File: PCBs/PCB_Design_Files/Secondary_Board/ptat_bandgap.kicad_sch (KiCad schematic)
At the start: 0 parts

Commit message: ptat_bandgap schematic on secondary board
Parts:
- added C1: .1u, Project Footprints:0603_capacitor, symbol Project_Symbols:0603_capacitor
- added IC1: TLV2333IDGKR, Project Footprints:TLV2333IDGKR, symbol Project_Symbols:TLV2333IDGKR
- added Q1, Q2: DMMT3904W-7-F, Project Footprints:DMMT3904W_Dual_NPN, symbol Project_Symbols:DMMT3904W-7-F
- added R3: 40k, Project Footprints:0603_resistor, symbol Project_Symbols:0603_resistor
- added R4: 2.5k, Project Footprints:0603_resistor, symbol Project_Symbols:0603_resistor
- added R5: 5k, Project Footprints:0603_resistor, symbol Project_Symbols:0603_resistor
- added R6, R7: 1k, Project Footprints:0603_resistor, symbol Project_Symbols:0603_resistor
- added R8: 103, Project Footprints:0603_resistor, symbol Project_Symbols:0603_resistor
- added R9: 2040, Project Footprints:0603_resistor, symbol Project_Symbols:0603_resistor
- added U1, U2, U3, U4: DMMT5401-7-F, Project Footprints:DMMT5401_Dual_PNP, symbol Project_Symbols:DMMT5401-7-F
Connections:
- new net: R7.2, U4.5 (E2)
- new net: Q1.1 (B2), Q1.6 (C2), Q2.1 (B2), Q2.2 (B1), Q2.3 (C1), Q2.6 (C2), R8.2
- new net: IC1.2 (-IN_A), IC1.6 (-IN_B), Q1.2 (B1), Q1.3 (C1), U1.1 (C1), U2.4 (C2)
- new net: R3.1, U1.2 (B1), U1.4 (C2)
- new net: IC1.5 (+IN_B), R8.1, U2.1 (C1)
- new net: IC1.7 (OUT_B), U1.3 (B2), U2.2 (B1), U2.3 (B2), U3.2 (B1), U3.3 (B2)
- new net: R6.2, U4.6 (E1)
- new net: IC1.3 (+IN_A), R9.1, U4.4 (C2)
- new net: IC1.1 (OUT_A), U4.2 (B1), U4.3 (B2)
- new net +3V3: C1.2, IC1.8 (V+), R6.1, R7.1, U1.5 (E2), U1.6 (E1), U2.5 (E2), U2.6 (E1), U3.5 (E2), U3.6 (E1)
- new net GND: C1.1, IC1.4 (V-), Q1.4 (E1), Q1.5 (E2), Q2.4 (E1), Q2.5 (E2), R3.2, R4.2, R5.2, R9.2
- new net V_bandgap: R4.1, U3.4 (C2), U4.1 (C1)
- new net V_ptat: R5.1, U3.1 (C1)
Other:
- note added: "1x NPN"
- note added: "3x NPN"
- note added: "Bandgap"
- note added: "Bandgap-PTAT Circuit"
- note added: "PTAT"
- note added: "Startup"

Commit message: updated bg_ptat
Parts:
- added C8: .1u, Project Footprints:0603_capacitor, symbol Project_Symbols:0603_capacitor
- added U7: TLV9002, Project Footprints:TLV9002, symbol Project_Symbols:TLV9002
- R4: value 2.5k -> 2.2k
- R8: value 103 -> 105
- R9: value 2040 -> 2050
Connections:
- net +3V3: now also C8.2, U7.8 (V+)
- net GND: now also C8.1, U7.4 (V-)
- net V_bandgap: now also U7.6 (IN2-), U7.7 (OUT2); no longer R4.1, U3.4 (C2), U4.1 (C1)
- net V_ptat: now also U7.1 (OUT1), U7.2 (IN1-); no longer R5.1, U3.1 (C1)
- new net Vbg: R4.1, U3.4 (C2), U4.1 (C1), U7.5 (IN2+)
- new net Vptat: R5.1, U3.1 (C1), U7.3 (IN1+)
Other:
- note added: "Buffer Output"
- moved on the sheet: C1, IC1, Q1, Q2, R3, R4, R5, R6, R7, R8, R9, U1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

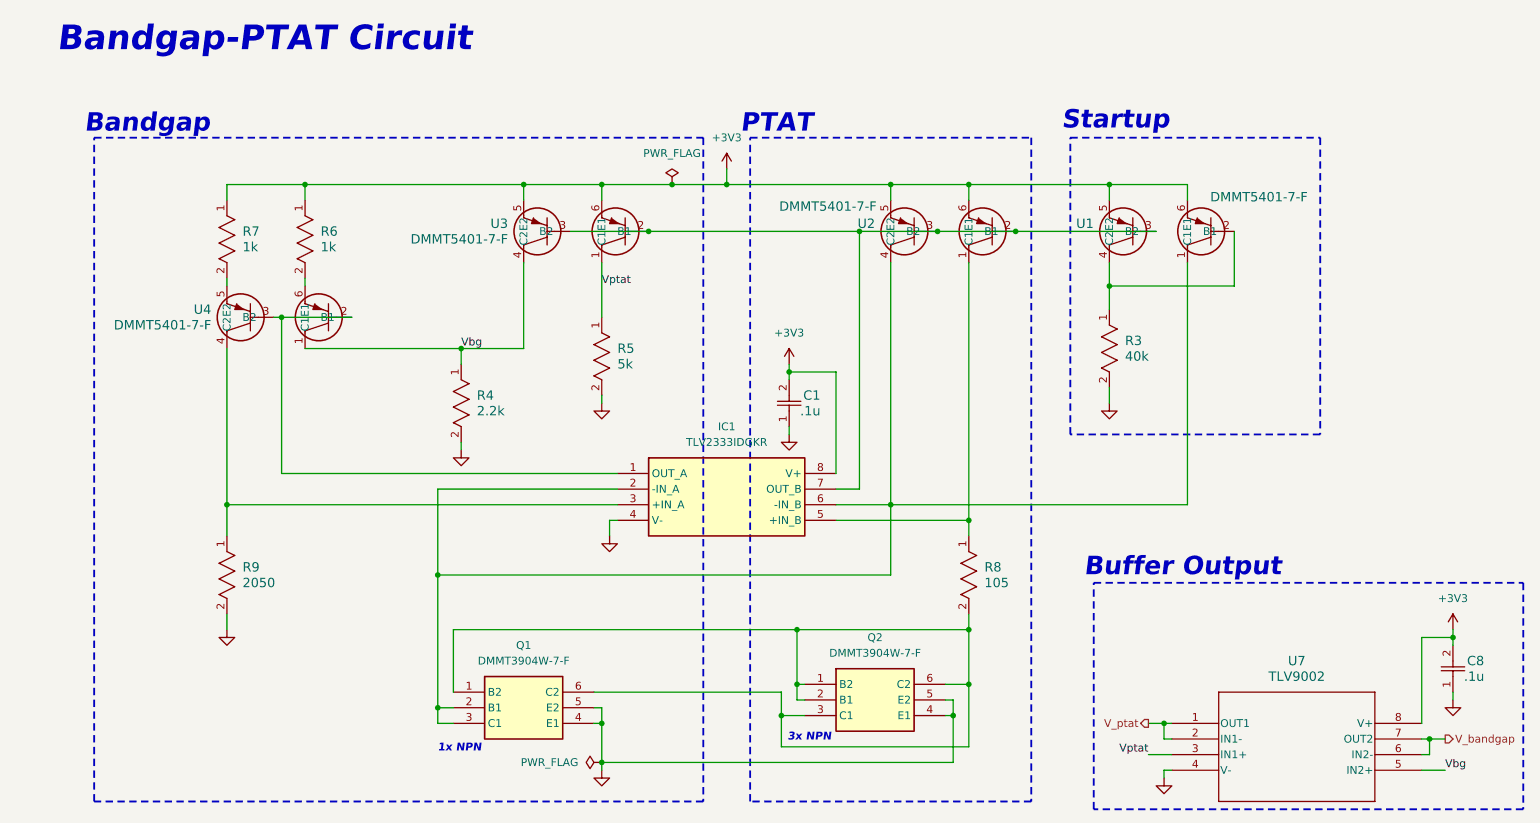
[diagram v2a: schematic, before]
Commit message: updated ptat_bandgap schematic and layout. Fixed +3v3 and +5V flags
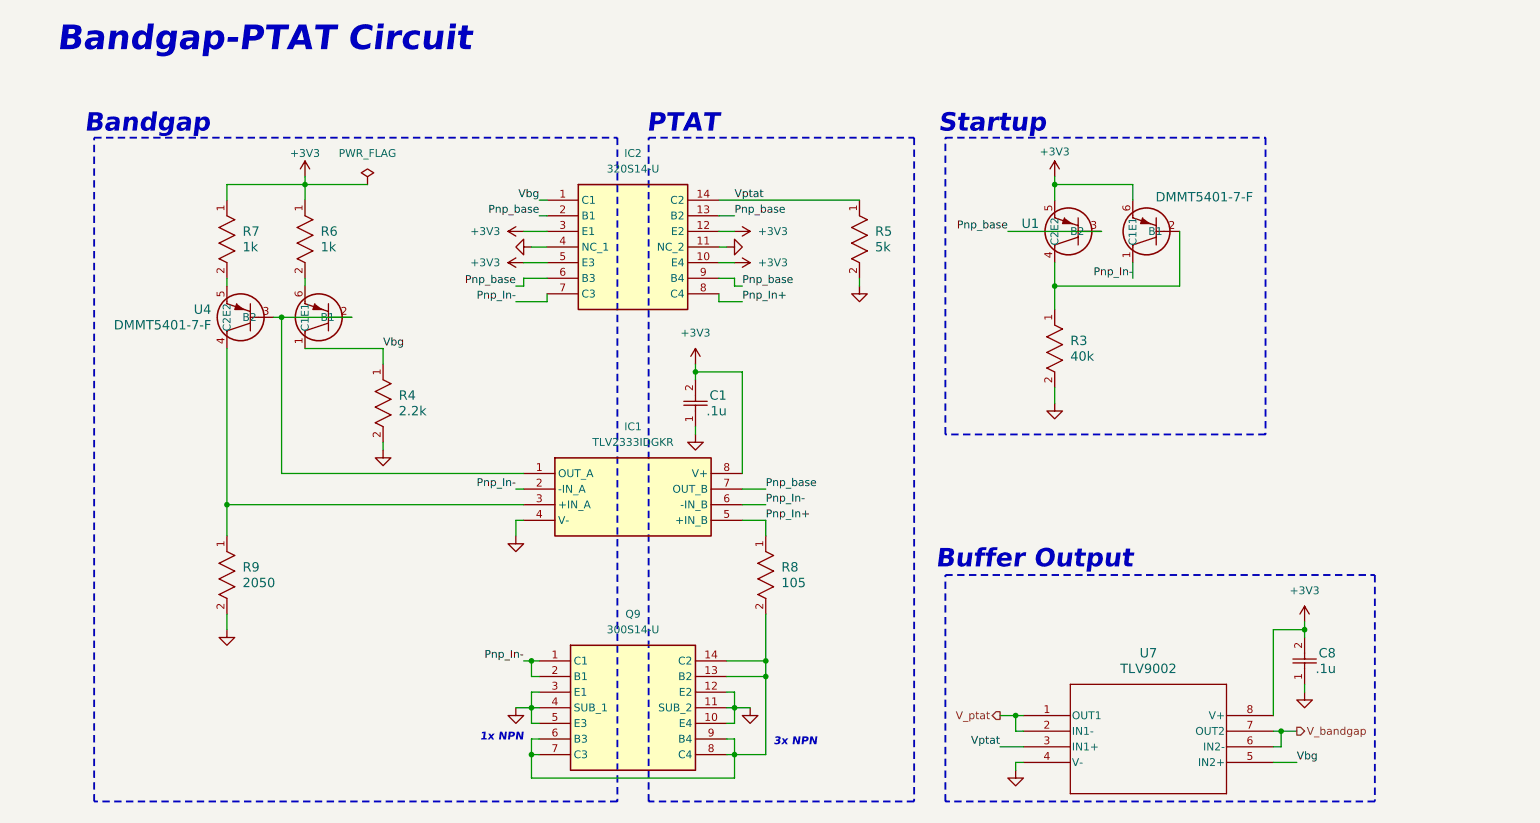
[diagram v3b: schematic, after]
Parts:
- removed Q1, Q2: DMMT3904W-7-F, Project Footprints:DMMT3904W_Dual_NPN, symbol Project_Symbols:DMMT3904W-7-F
- removed U2, U3: DMMT5401-7-F, Project Footprints:DMMT5401_Dual_PNP, symbol Project_Symbols:DMMT5401-7-F
- added IC2: 320S14-U, Project Footprints:That320_pnp, symbol Project_Symbols:320S14-U
- added Q9: 300S14-U, Project Footprints:That300_npn, symbol Project_Symbols:300S14-U
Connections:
- net +3V3: now also IC2.10 (E4), IC2.12 (E2), IC2.3 (E1), IC2.5 (E3)
- net GND: now also IC2.11 (NC_2), IC2.4 (NC_1), Q9.10 (E4), Q9.11 (SUB_2), Q9.12 (E2), Q9.3 (E1), Q9.4 (SUB_1), Q9.5 (E3)
- net Vbg: now also IC2.1 (C1)
- net Vptat: now also IC2.14 (C2)
- net at R8.2: now also Q9.13 (B2), Q9.14 (C2), Q9.6 (B3), Q9.7 (C3), Q9.8 (C4), Q9.9 (B4)
- net Pnp_In-: now reaches IC1.2 (-IN_A), IC1.6 (-IN_B), U1.1 (C1)
- net Pnp_In-: now also IC2.7 (C3), Q9.1 (C1), Q9.2 (B1)
- net Pnp_In+: now reaches IC1.5 (+IN_B), R8.1
- net Pnp_In+: now also IC2.8 (C4)
- net Pnp_base: now reaches IC1.7 (OUT_B), U1.3 (B2)
- net Pnp_base: now also IC2.13 (B2), IC2.2 (B1), IC2.6 (B3), IC2.9 (B4)
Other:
- moved on the sheet: C1, C8, IC1, R3, R4, R5, R8, U1, U7

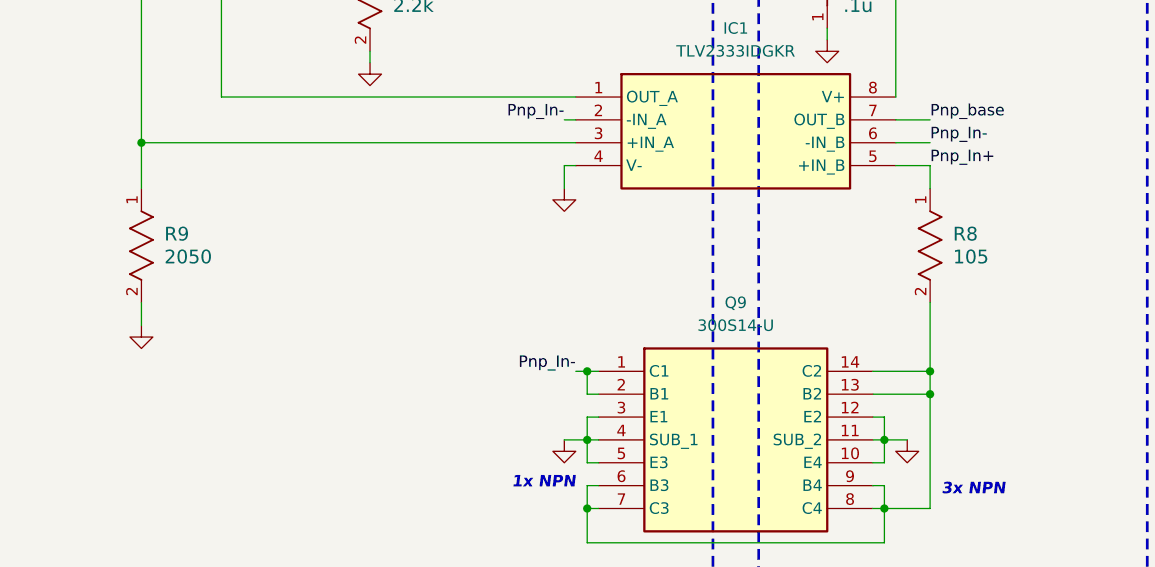
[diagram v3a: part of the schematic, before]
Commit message: updated soldered values
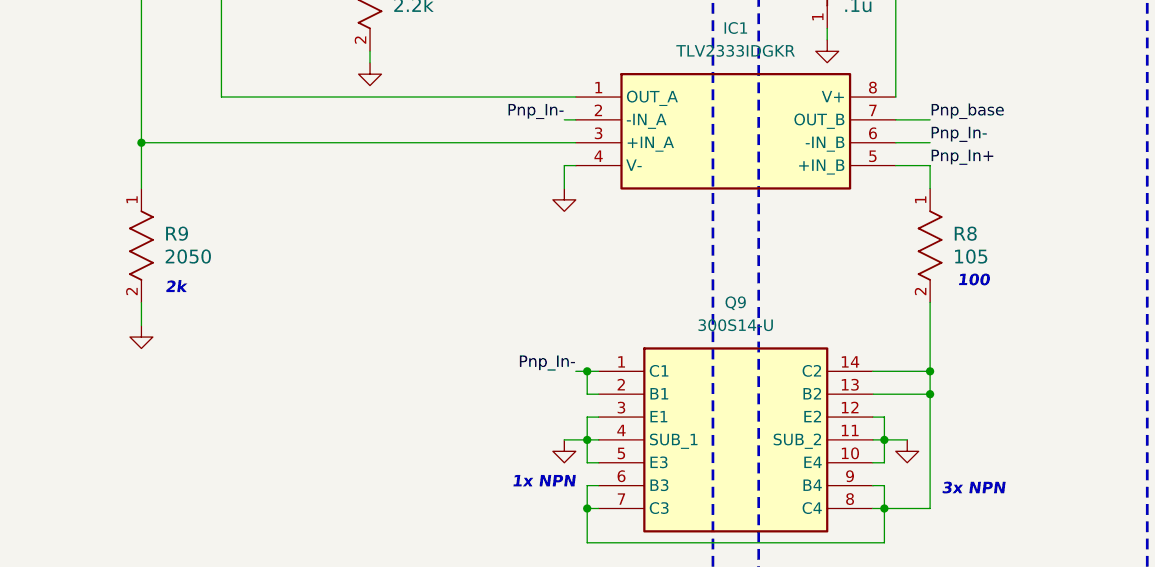
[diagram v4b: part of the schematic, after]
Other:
- note added: "100"
- note added: "2k"
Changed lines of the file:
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@@
+		)
+	)
+	(text "100\n\n"
+		(exclude_from_sim no)
+		(at 134.366 110.49 0)
+		(effects
+			(font
+				(size 1.27 1.27)
+				(thickness 0.254)
+				(bold yes)
+				(italic yes)
+			)
+		)
+	)
+	(text "2k\n"
+		(exclude_from_sim no)
+		(at 45.72 110.236 0)
+		(effects
+			(font
+				(size 1.27 1.27)
+				(thickness 0.254)
+				(bold yes)
+				(italic yes)
+			)
 		)
 	)
